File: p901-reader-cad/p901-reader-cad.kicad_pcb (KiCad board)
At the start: 2 copper layers, 91.8 x 93.2 mm, 20 parts, among them J1 DE15 (F), J2 5.5mm Barrel (F), U1 MAX232, U2 TPS63060, U3 DOIT ESP32 DevKit v1

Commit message: bump: JLC selections
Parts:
- added C10: 22 μF, Capacitor_SMD:C_0805_2012Metric_Pad1.18x1.45mm_HandSolder, F.Cu at (147.1, 95.0)
- C7: value 22 μF -> 22 μF (±10%); footprint Capacitor_SMD:C_0805_2012Metric_Pad1.18x1.45mm_HandSolder -> Capacitor_SMD:C_1206_3216Metric_Pad1.33x1.80mm_HandSolder
- C9: value 68 μF -> 47 μF
- R2: value 111 kΩ -> 110 kΩ
- moved C7 0.66 mm to (157.8, 93.7)
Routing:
- net +9V: track 41.3 -> 34.0 mm
- net GND: track 8.63 -> 9.90 mm, vias 961 -> 1003

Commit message: fix DRC again
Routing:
- net +9V: track 34.0 -> 41.9 mm
- net GND: vias 1003 -> 985
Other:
- board text added: "ANTENNA THIS SIDE"

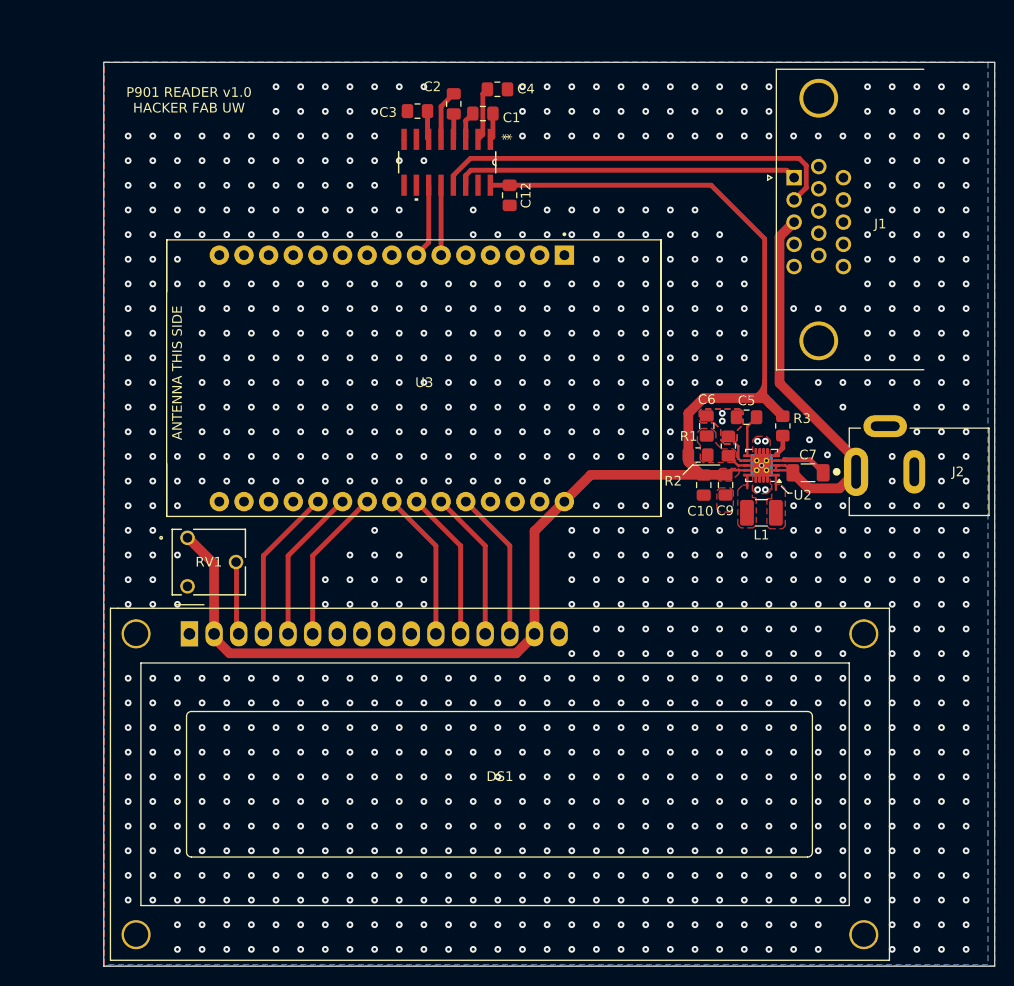
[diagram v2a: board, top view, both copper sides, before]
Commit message: update to KiCAD 10.0, reroute against official ESP footprints
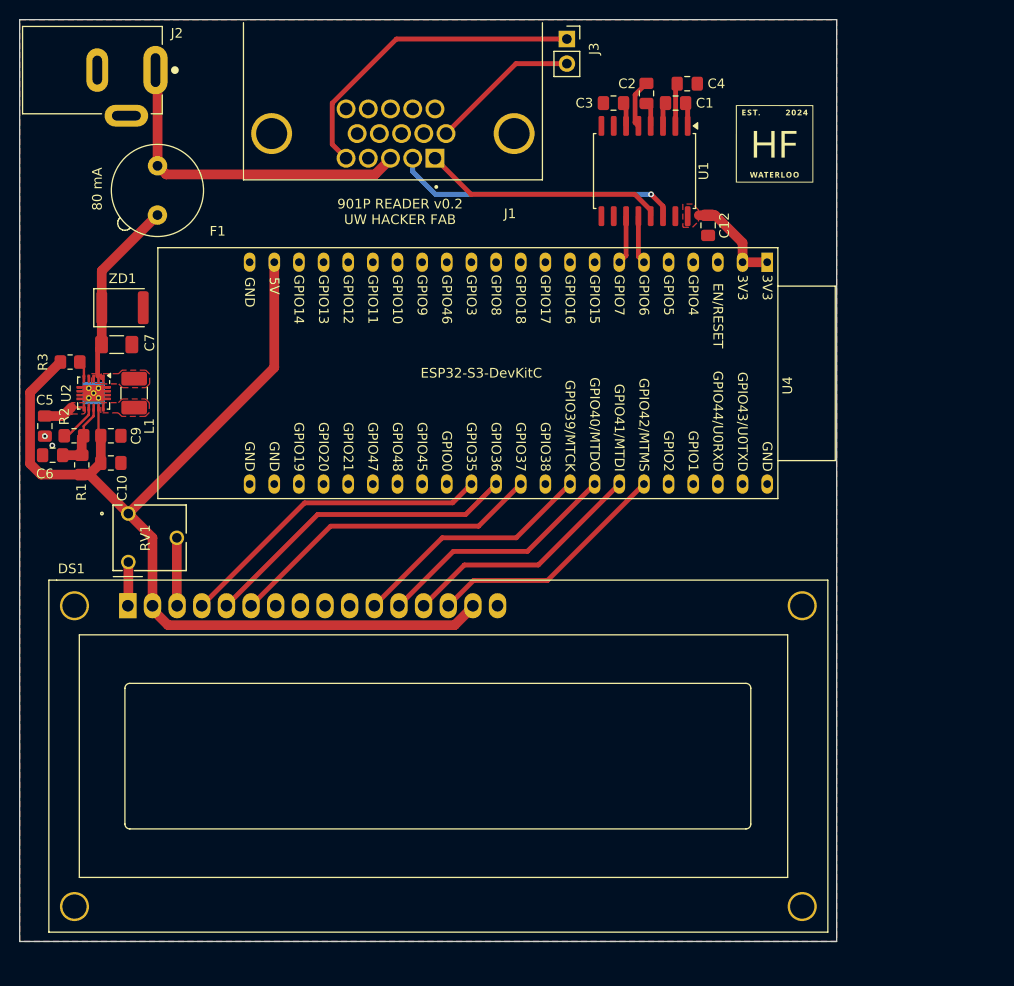
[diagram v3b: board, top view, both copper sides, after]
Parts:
- removed U3: DOIT ESP32 DevKit v1, ESP32-DEVKIT-V1:MODULE_ESP32_DEVKIT_V1
- added F1: 80 mA, Fuse:Fuseholder_TR5_Littelfuse_No560_No460, F.Cu at (90.8, 62.1)
- added G***: LOGO, hackerfab_logo:hackerfab_logo, F.Cu at (154.4, 59.8)
- added J3: ANALOG, Connector_PinSocket_2.54mm:PinSocket_1x02_P2.54mm_Vertical, F.Cu at (133.0, 49.0)
- added U4: ESP32-S3-DevKitC, PCM_Espressif:ESP32-S3-DevKitC, F.Cu at (153.6, 72.0)
- added ZD1: Vz=9 V, Diode_SMD:D_1812_4532Metric, F.Cu at (87.2, 76.7)
- C1, C2, C3, C4: value 1 μF -> 100 nF
- J1: footprint Connector_Dsub:DSUB-15-HD_Socket_Horizontal_P2.29x2.54mm_EdgePinOffset8.35mm_Housed_MountingHolesOffset10.89mm -> Amphenol_P154XLF:AMPHENOL_10090926-P154XLF
- U1: value MAX232 -> MAX3232; footprint TI_MAX232Dx:D16 -> Package_SO:SOIC-16W_7.5x10.3mm_P1.27mm
- moved J2 83.2 mm to (90.6, 52.2), turned to 180 degrees
- moved R3 73.7 mm to (81.8, 82.3), turned to 0 degrees
- moved C7 72.5 mm to (86.6, 80.5)
- moved C5 72.3 mm to (79.2, 88.9), turned to -90 degrees
- moved U2 69.2 mm to (84.2, 85.5), turned to -90 degrees
- moved C6 67.5 mm to (80.0, 91.9), turned to 180 degrees
- moved R2 67.4 mm to (82.2, 89.9), turned to 180 degrees
- moved L1 65.8 mm to (88.4, 85.5), turned to -90 degrees
- moved C9 63.6 mm to (86.0, 89.9), turned to 0 degrees
- moved R1 63.5 mm to (83.0, 92.9), turned to 90 degrees
- moved C10 61.1 mm to (86.0, 92.7), turned to 0 degrees
- moved J1 41.6 mm to (115.1, 58.7), turned to 180 degrees
- moved C12 20.7 mm to (147.6, 68.2)
- moved U1 20.4 mm to (141.0, 62.6)
- moved C3 20.2 mm to (137.8, 55.6), turned to 180 degrees
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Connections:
- C12 pad 1: +5V -> +3V3
- C3 pad 1: GND -> Net-(U1-VS-)
- C3 pad 2: Net-(U1-VS-) -> GND
- C7 pad 1: +9V -> Net-(U2-EN)
- J1 pad 1: Net-(U1-T1OUT) -> Net-(U1-R1IN)
- J1 pad 2: Net-(U1-R1IN) -> Net-(U1-T1OUT)
- J1 pad 5: unconnected-(J1-Pad5) -> /ANALOG_V+
- J1 pad 6: unconnected-(J1-Pad6) -> /ANALOG_V-
- U1 pad 16: +5V -> +3V3
- U2 pad 2: +9V -> Net-(U2-EN)
- U2 pad 3: +9V -> Net-(U2-EN)
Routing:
- net +5V: track 146.9 -> 109.2 mm
- net /ANALOG_V+: track 0.00 -> 33.2 mm
- net Net-(U2-EN): track 0.00 -> 19.1 mm
- net Net-(U1-R1IN): track 42.5 -> 25.1 mm
- net /LCD_E: track 16.0 -> 33.0 mm
- net /LCD_RW: track 16.0 -> 33.0 mm
- net /LCD_RS: track 16.0 -> 33.0 mm
- net /ANALOG_V-: track 0.00 -> 15.4 mm
- net +3V3: track 0.00 -> 10.2 mm
- net /LCD_D5: track 15.5 -> 25.4 mm
- net /LCD_D7: track 15.5 -> 25.4 mm
- net /LCD_D6: track 15.5 -> 25.4 mm
- net /LCD_D4: track 15.5 -> 25.4 mm
- net +9V: track 41.9 -> 35.1 mm
- net Net-(U1-T1OUT): track 35.4 -> 29.7 mm, vias 0 -> 1
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- added copper zone on F.Cu, net +3V3
- added copper zone on F.Cu, net Net-(U2-EN)
- added copper zone on F.Cu, net Net-(U2-VAUX)
- removed copper zone on F.Cu, net +5V
- removed copper zone on F.Cu, net Net-(U2-FB)
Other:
- board size 91.8 x 93.2 mm -> 84.2 x 95 mm
- board text added: "901P READER v0.2 UW HACKER FAB"
- board text removed: "ANTENNA THIS SIDE"
- board text removed: "P901 READER v1.0 HACKER FAB UW"

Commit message: add stitching vias
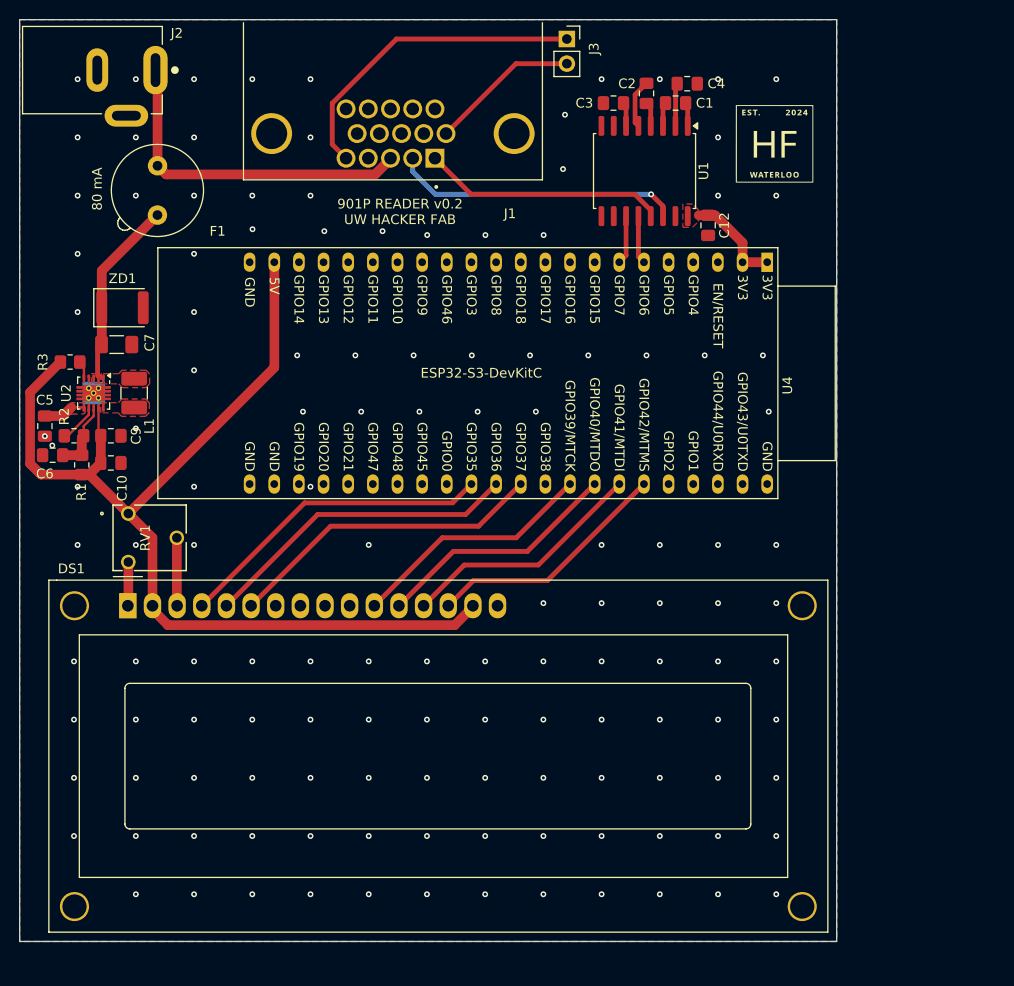
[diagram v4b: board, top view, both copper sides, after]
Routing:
- net GND: vias 2 -> 132
